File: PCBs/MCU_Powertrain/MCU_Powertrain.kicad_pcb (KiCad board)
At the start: 4 copper layers, 157 parts, among them J1 PHASE_A, J2 PHASE_B, J3 PHASE_C, J4 Big Conn, J5 Pogo Conn, J6 Conn CAN, J7 PWRIN, Q1 SIZF906DT, Q2 SIZF906DT, Q3 SIZF906DT, SW1 SW_Push, SW2 SW_Push, U1 DRV8305, U2 SN65HVD232, U3 MCP2515, U4 LMR16006XDDC, U5 TMS320F28027F, U6 SN74LVC2G07, U7 SN74LVC2G07, Y1 20MHz

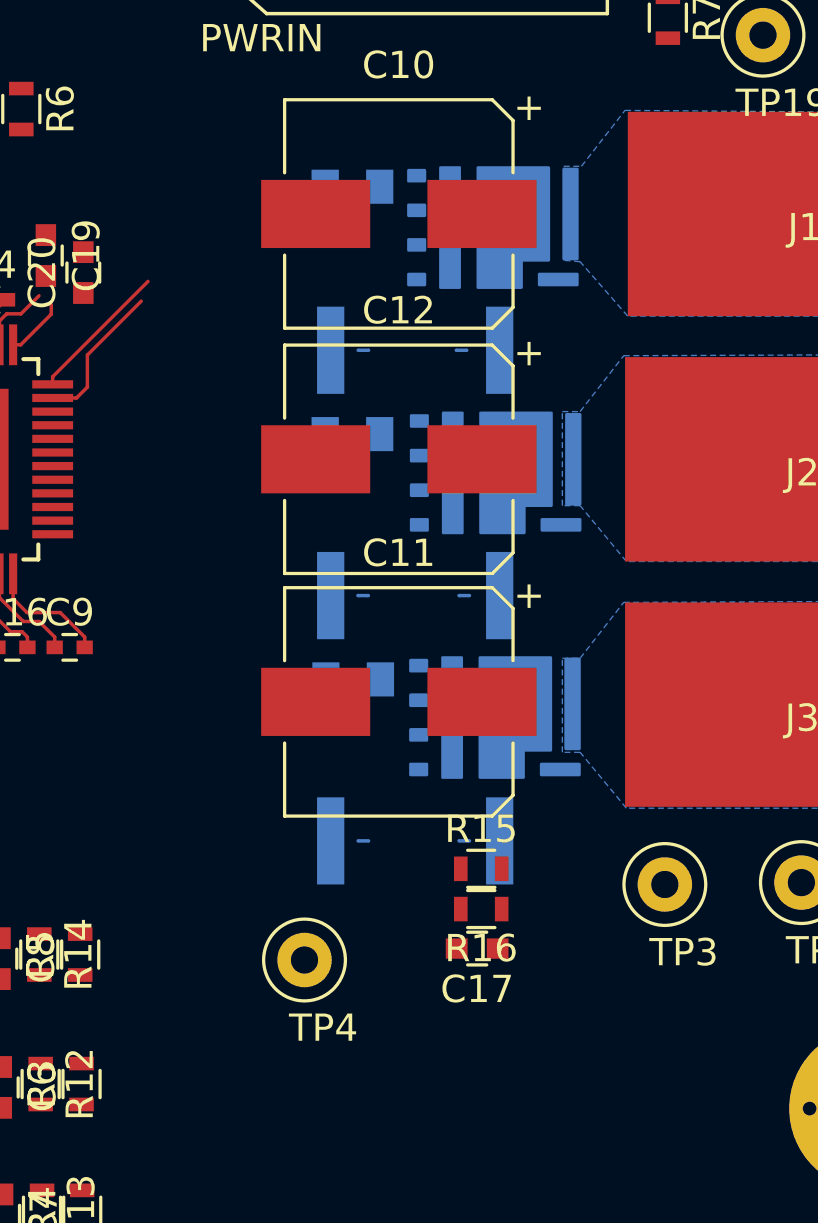
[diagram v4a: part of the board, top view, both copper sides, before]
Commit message: Routing
- Small routing changes, mostly to the inverter section
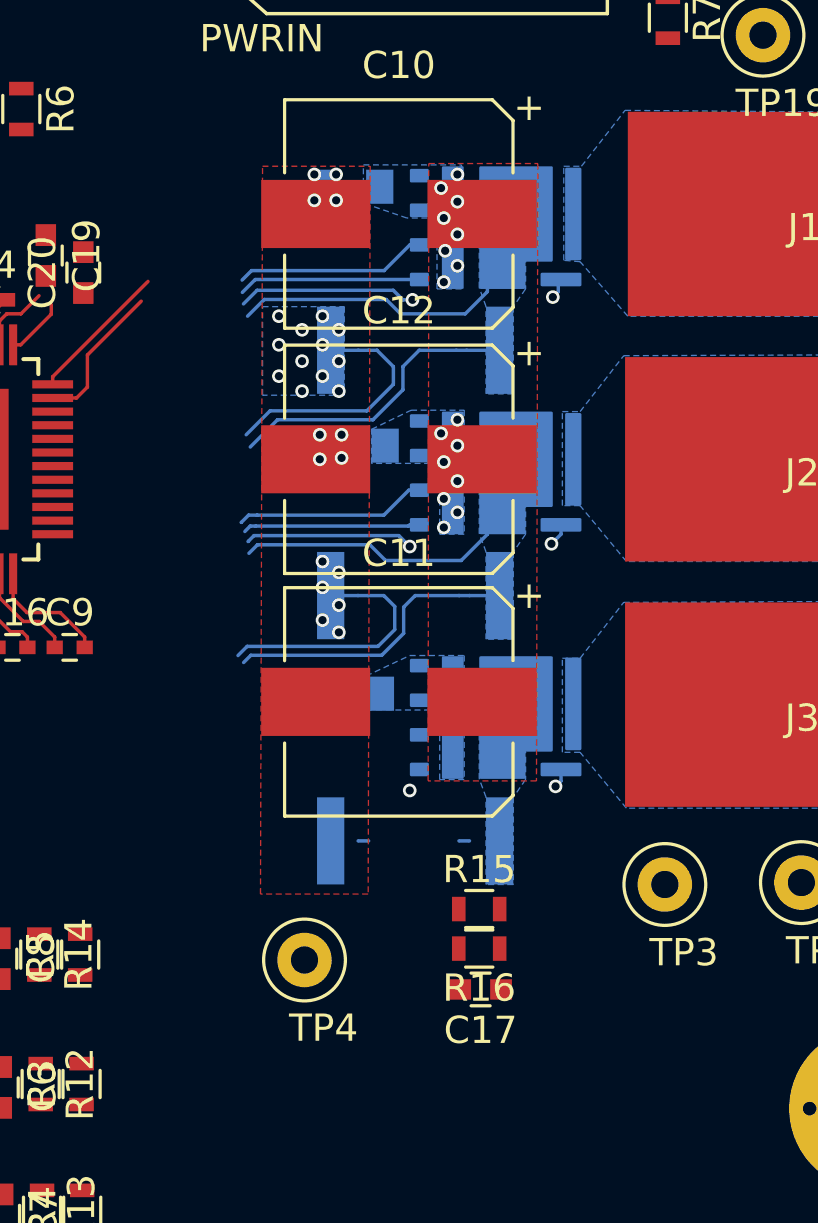
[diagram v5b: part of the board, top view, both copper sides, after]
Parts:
- moved C17 1.51 mm to (92.3, 122.0)
- moved R15 1.48 mm to (92.2, 119.0)
- moved R16 1.45 mm to (92.2, 120.5)
- moved C15 0.52 mm to (87.6, 111.1)
- moved C14 0.47 mm to (87.8, 102.0)
- moved Q3 0.10 mm to (89.9, 94.0)
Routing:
- net /Powertrain/SL_A: track 0.00 -> 13.2 mm
- net /Powertrain/SL_B: track 0.00 -> 12.9 mm
- net /Powertrain/GL_A: track 0.00 -> 12.5 mm, vias 0 -> 2
- net /Powertrain/GL_B: track 0.00 -> 12.3 mm, vias 0 -> 2
- net /Powertrain/SN1: track 3.88 -> 13.4 mm
- net /Powertrain/SN2: track 3.08 -> 12.6 mm
- net /Powertrain/SP2: track 3.58 -> 11.7 mm
- net /Powertrain/SP1: track 4.50 -> 12.5 mm
- net /Powertrain/SH_A: track 5.41 -> 12.4 mm
- net /Powertrain/SH_B: track 0.00 -> 7.02 mm
- net /Powertrain/GH_A: track 5.22 -> 11.8 mm
- net /Powertrain/GH_B: track 0.00 -> 6.51 mm
- net /Powertrain/GL_C: track 0.00 -> 6.11 mm, vias 0 -> 2
- net GND: track 1.25 -> 3.26 mm, vias 1 -> 27
- net +BATT: vias 0 -> 16
- added copper zone on B.Cu, net +BATT
- added copper zone on F.Cu, net +BATT
- added copper zone on B.Cu, net /Powertrain/SL_A
- added copper zone on B.Cu, net /Powertrain/SL_B
- added copper zone on B.Cu, net /Powertrain/SL_C
- added copper zone on B.Cu, net GND
- added copper zone on F.Cu, net GND

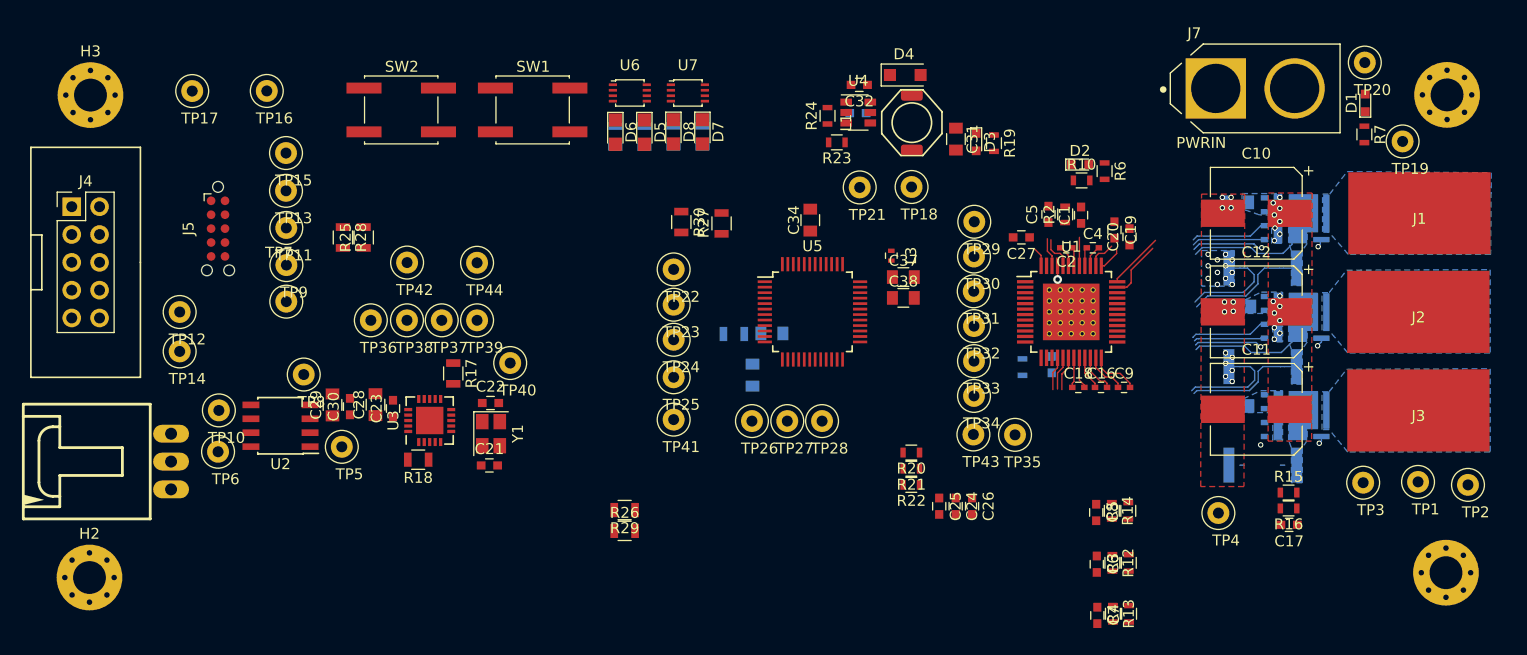
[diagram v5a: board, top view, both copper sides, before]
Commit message: Routing
- Routed most of DRV and TI chips
- FETs are done
- Added board outline
- Added power and ground planes
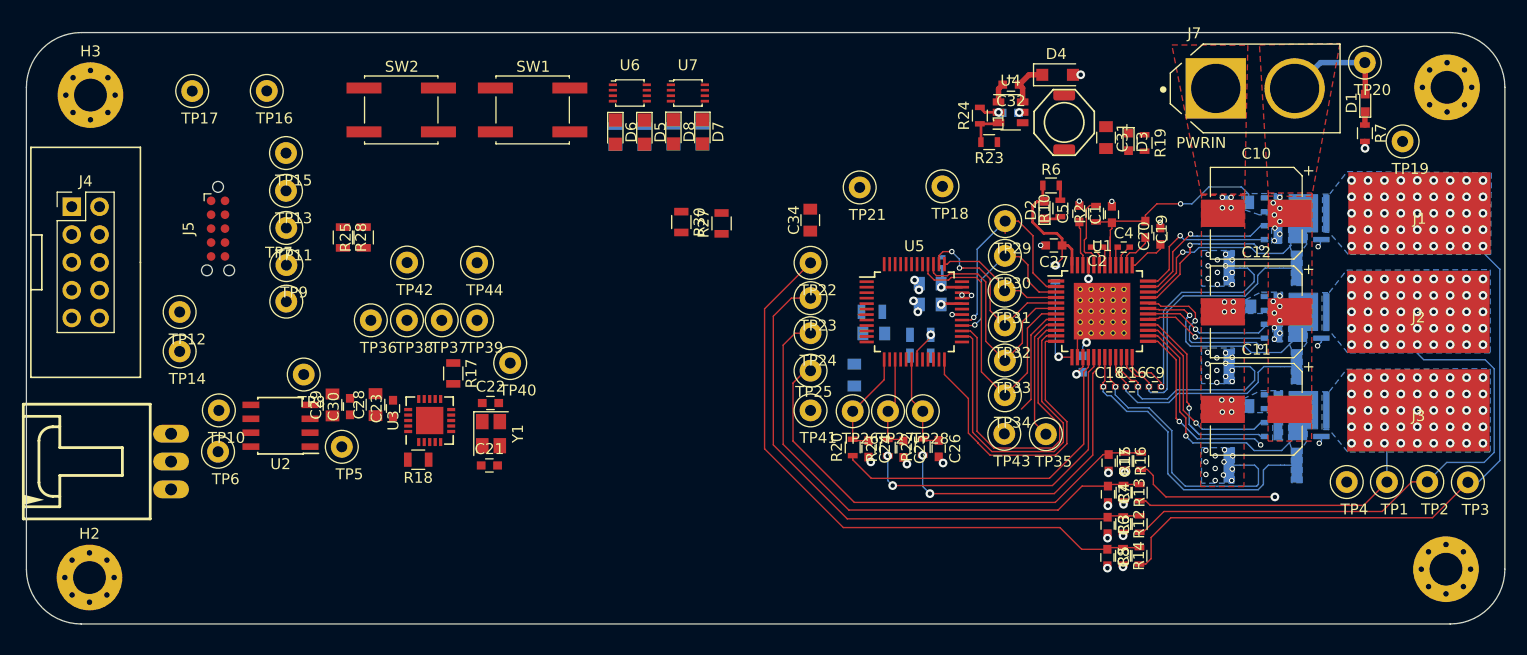
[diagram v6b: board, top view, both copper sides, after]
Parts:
- C37, C38, L3, R26, R29: moved to B.Cu
- TP1, TP10, TP11, TP12, TP13, TP14, TP15, TP16, TP17, TP18, TP19, TP2, TP20, TP21, TP22, TP23, TP24, TP25, TP26, TP27, TP28, TP29, TP3, TP30, TP31, TP32, TP33, TP34, TP35, TP36, TP37, TP38, TP39, TP4, TP40, TP41, TP42, TP43, TP44, TP5, TP6, TP7, TP8, TP9: footprint Testpoints:TestPoint_Loop_D1.80mm_Drill1.0mm_Beaded -> MCU_Powertrain:TestPoint_Loop_D1.80mm_Drill1.0mm_Beaded
- moved R26 32.4 mm to (58.6, 104.6)
- moved R29 30.5 mm to (58.6, 106.5)
- moved C17 17.4 mm to (75.8, 116.3), turned to 270 degrees
- moved R16 15.6 mm to (77.3, 116.1), turned to 270 degrees
- moved D3 13.9 mm to (77.6, 87.0)
- moved L1 13.9 mm to (71.8, 85.2)
- moved R24 13.9 mm to (64.1, 84.6)
- moved U4 13.9 mm to (66.9, 84.3)
- moved C33 13.9 mm to (66.8, 84.3)
- moved D4 13.9 mm to (71.2, 80.9)
- moved R23 13.9 mm to (64.9, 87.0)
- moved C32 13.9 mm to (66.9, 81.8)
- moved R15 13.8 mm to (78.8, 116.1), turned to 90 degrees
- moved R19 13.8 mm to (79.1, 87.1)
- moved C31 13.7 mm to (75.6, 86.6)
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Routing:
- net /Powertrain/Phase_A: track 0.00 -> 58.2 mm, vias 0 -> 45
- net /TI_MCU/ADCINA7: track 0.00 -> 56.8 mm
- net /TI_MCU/ADCINA3: track 0.00 -> 53.0 mm
- net /Powertrain/Phase_B: track 0.00 -> 51.4 mm, vias 0 -> 45
- net /TI_MCU/ADCINA1: track 0.00 -> 48.0 mm
- net +BATT: track 2.60 -> 47.3 mm, vias 16 -> 19
- net /TI_MCU/ADCINA0: track 0.00 -> 43.3 mm
- net /Powertrain/SPI_MOSI: track 0.00 -> 30.7 mm
- net /Powertrain/SPI_MISO: track 0.00 -> 30.5 mm
- net /Powertrain/SPI_CLK: track 0.00 -> 29.0 mm
- net /Powertrain/ISEN_A_DRV: track 3.08 -> 31.6 mm
- net /Powertrain/ISEN_B_DRV: track 3.06 -> 30.8 mm, vias 0 -> 2
- net /Powertrain/Phase_C: track 0.00 -> 27.6 mm, vias 0 -> 45
- net /TI_MCU/EPWM3B: track 0.00 -> 27.6 mm
- net /Powertrain/ISEN_C_DRV: track 3.15 -> 29.3 mm, vias 0 -> 2
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- added copper zone on In2.Cu, net +3V3
- added copper zone on In2.Cu, net +BATT
- added copper zone on In1.Cu, net GND
- added copper zone on In2.Cu, net GND
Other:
- board outline added: 135 x 54 mm

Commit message: More Routing
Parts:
- C34: moved to B.Cu
- moved D5 20.1 mm to (53.5, 86.4)
- moved D6 20.1 mm to (50.8, 86.4)
- moved R31 20.1 mm to (53.5, 86.8)
- moved R32 20.1 mm to (50.8, 86.8)
- moved U7 20.1 mm to (57.5, 82.8)
- moved D7 20.1 mm to (58.8, 86.4)
- moved D8 20.1 mm to (56.1, 86.4)
- moved R33 20.1 mm to (56.1, 86.8)
- moved R34 20.1 mm to (58.8, 86.8)
- moved U6 20.1 mm to (52.1, 82.8)
- moved C35 15.8 mm to (60.4, 94.5), turned to 90 degrees
- moved TP21 10.9 mm to (63.9, 89.4)
- moved C34 9.38 mm to (57.9, 95.5)
- moved TP18 7.06 mm to (67.5, 89.3)
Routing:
- net /GPIO28: track 11.4 -> 52.1 mm, vias 0 -> 4
- net +BATT: track 47.3 -> 78.8 mm
- net /TI_MCU/GPIO7: track 0.00 -> 18.3 mm, vias 0 -> 2
- net /Powertrain/EN_GATE: track 0.00 -> 17.4 mm, vias 0 -> 2
- net /Powertrain/SPI_CS_0: track 11.7 -> 23.7 mm, vias 0 -> 2
- net +3V3: track 12.7 -> 23.4 mm, vias 1 -> 39
- net /TI_MCU/ADCINA0: track 43.3 -> 50.5 mm
- net /TI_MCU/ADCINA7: track 56.8 -> 63.7 mm
- net /TI_MCU/CAN_INT: track 0.00 -> 5.85 mm
- net /TI_MCU/ADCINA1: track 48.0 -> 53.6 mm
- net GND: track 23.8 -> 29.4 mm, vias 75 -> 84
- net /TI_MCU/ADCINA3: track 53.0 -> 57.9 mm
- net /TI_MCU/SPI_CS_1: track 0.00 -> 3.99 mm
- net Net-(C36-Pad1): track 0.00 -> 3.86 mm, vias 0 -> 1
- net /TRST: track 0.00 -> 3.81 mm
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- added copper zone on F.Cu, net +3V3
- added copper zone on F.Cu, net Net-(C32-Pad1)

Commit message: Initial Routing Complete
- Connected all nets, no DRC errors
- Still need to investigate the CAN logic level and add in a termination resistor
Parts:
- moved SW2 59.9 mm to (53.2, 126.8)
- moved TP7 30.3 mm to (31.1, 102.6)
- moved J5 30.3 mm to (24.8, 96.2)
- moved TP11 30.3 mm to (31.0, 96.2)
- moved TP13 30.3 mm to (31.0, 92.8)
- moved TP15 30.3 mm to (31.0, 89.3)
- moved TP9 30.3 mm to (31.0, 99.6)
- moved TP16 28.4 mm to (27.2, 80.6)
- moved TP17 28.4 mm to (20.4, 80.6)
- moved R28 27.8 mm to (33.7, 97.2)
- moved R25 27.8 mm to (35.6, 97.2)
- moved J6 27.8 mm to (10.2, 112.8)
- moved J4 26.9 mm to (9.20, 96.1)
- moved H3 26.7 mm to (9.55, 81.8)
- moved H2 26.7 mm to (9.45, 126.8)
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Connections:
- Y1 pad 2: Net-(C21-Pad1) -> GND
- Y1 pad 3: (no net) -> Net-(C21-Pad1)
- Y1 pad 4: (no net) -> GND
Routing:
- net /TDO: track 0.00 -> 98.6 mm, vias 0 -> 2
- net /TCK: track 0.00 -> 82.5 mm, vias 0 -> 3
- net /TMS: track 0.00 -> 74.5 mm, vias 0 -> 1
- net /TDI: track 0.00 -> 63.8 mm, vias 0 -> 4
- net /GPIO28: track 52.1 -> 112.9 mm
- net /TRST: track 3.81 -> 61.7 mm, vias 0 -> 1
- net /GPIO29: track 3.66 -> 60.5 mm, vias 0 -> 1
- net /TI_MCU/SPI_CS_1: track 3.99 -> 55.6 mm, vias 0 -> 1
- net /TI_MCU/CAN_INT: track 5.85 -> 55.6 mm, vias 0 -> 1
- net /Powertrain/SPI_MOSI: track 34.4 -> 81.2 mm, vias 0 -> 1
- net /Powertrain/PWRGD: track 11.8 -> 58.2 mm, vias 1 -> 4
- net /Powertrain/SPI_MISO: track 34.0 -> 71.7 mm, vias 0 -> 1
- net /Powertrain/SPI_CLK: track 32.5 -> 63.5 mm, vias 0 -> 1
- net /TI_MCU/EPWM1B: track 15.5 -> 44.2 mm, vias 1 -> 2
- net /TI_MCU/EPWM1A: track 21.5 -> 47.8 mm, vias 1 -> 2
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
